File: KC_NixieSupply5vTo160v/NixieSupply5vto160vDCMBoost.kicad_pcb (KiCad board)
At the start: 2 copper layers, 38.2 x 37.9 mm, 47 parts, among them J1 Screw_Terminal_01x04, J2 CONN_01X01, J3 CONN_01X01, J4 CONN_01X01, J5 CONN_01X01, P1 USB_OTG, Q1 FDS2672CT, Q26 MMBTA42, U1 UCC3803

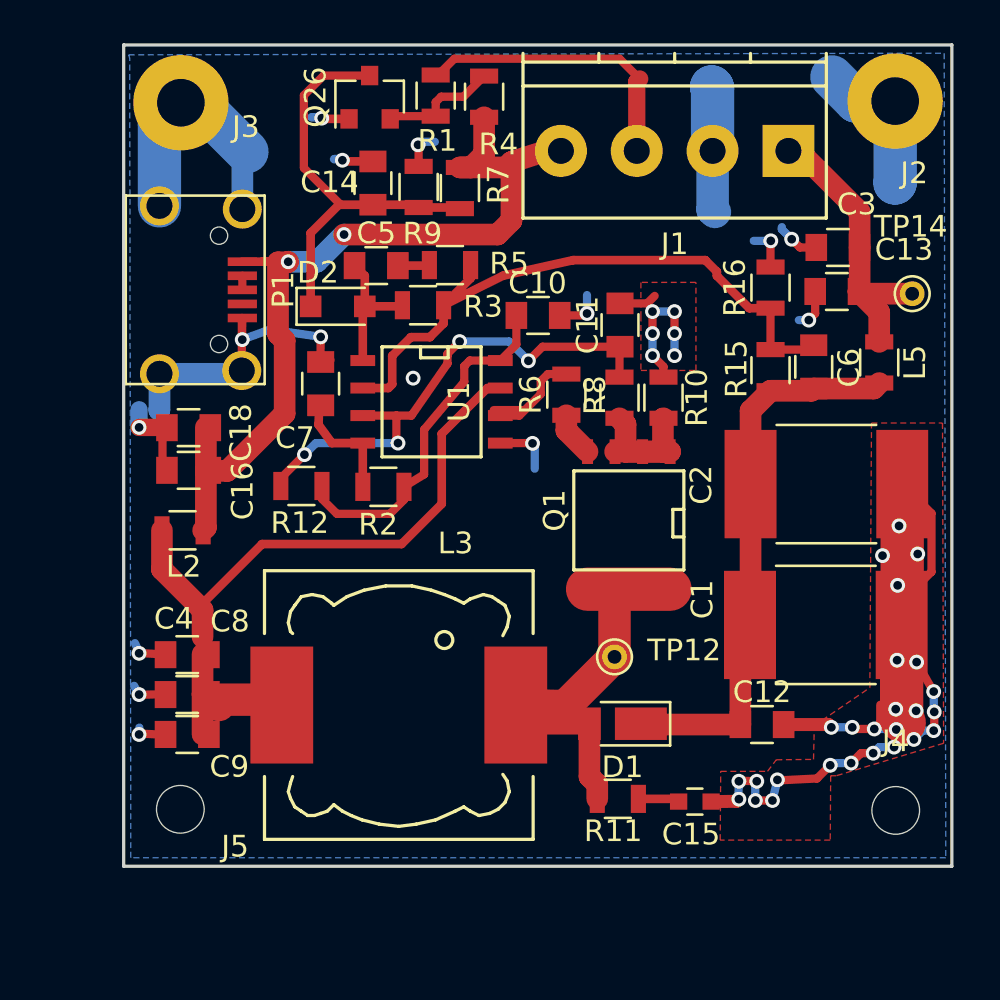
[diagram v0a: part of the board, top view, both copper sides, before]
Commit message: Latest updates for the verification Blog
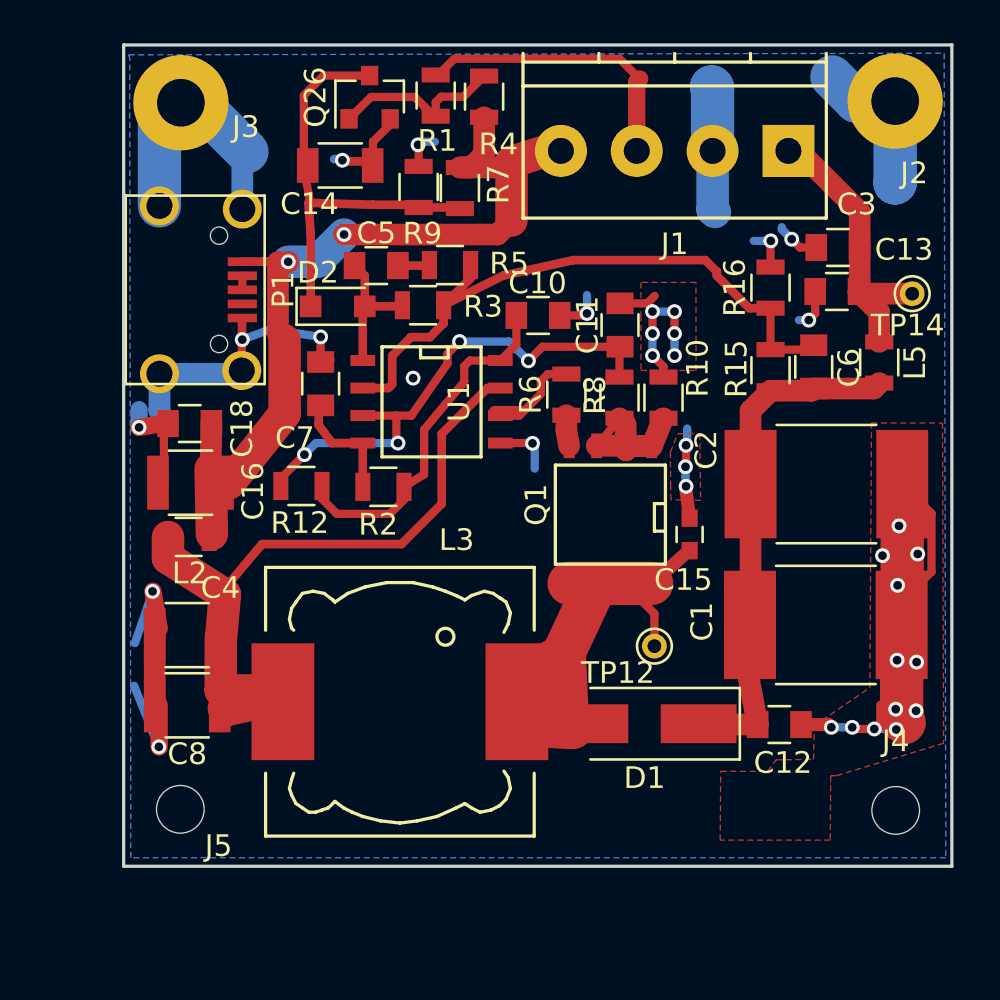
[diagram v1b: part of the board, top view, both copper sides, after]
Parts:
- removed C9: 47uF 10v, Capacitors_SMD:C_0805
- removed R11: 20 0.5W, Resistors_SMD:R_0805
- C14: value 47uF 10v -> 47uF 16v; footprint Capacitors_SMD:C_0805 -> Capacitors_SMD:C_1206
- C15: value 47pF 250v -> 560pF 250v
- C16, C4, C8: value 47uF 10v -> 100uF 16v; footprint Capacitors_SMD:C_0805 -> Capacitors_SMD:C_1210
- C7: value 330pF -> 430pF
- D1: value DFLS1200-7 -> ES1D; footprint Diodes_SMD:D_PowerDI-123 -> Diodes_SMD:D_SMA_Handsoldering
- Q26: value MMBTA42 -> MMBT42
- R12: value 8.2k -> 4.12k
- R6: value 10 -> 0 Ohm
- moved C15 12.3 mm to (162.2, 95.8), turned to 90 degrees
- moved TP12 1.91 mm to (160.6, 101.0)
- moved C14 1.72 mm to (146.1, 78.8), turned to 0 degrees
- moved D1 1.02 mm to (160.1, 104.5)
- moved C4 0.90 mm to (139.0, 100.4)
- moved Q1 0.89 mm to (158.5, 94.9)
- moved C12 0.80 mm to (166.3, 104.6)
- moved C16 0.58 mm to (139.2, 93.4)
- moved C8 0.50 mm to (139.0, 103.7)
- moved L2 0.41 mm to (139.1, 95.9)
- moved C18 0.20 mm to (139.1, 90.7)
- moved L3 0.16 mm to (148.8, 103.5)
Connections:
- D1 pad 2: Net-(D1-Pad2) -> Net-(C15-Pad1)
- L3 pad 1: Net-(D1-Pad2) -> Net-(C15-Pad1)
- Q1 pad 5: Net-(D1-Pad2) -> Net-(C15-Pad1)
- Q1 pad 6: Net-(D1-Pad2) -> Net-(C15-Pad1)
- Q1 pad 7: Net-(D1-Pad2) -> Net-(C15-Pad1)
- Q1 pad 8: Net-(D1-Pad2) -> Net-(C15-Pad1)
- Q26 pad 1: GND -> Net-(Q26-Pad1)
- Q26 pad 2: Net-(Q26-Pad2) -> GND
- R1 pad 1: Net-(Q26-Pad2) -> Net-(Q26-Pad1)
- R4 pad 1: Net-(Q26-Pad2) -> Net-(Q26-Pad1)
- TP12 pad 1: Net-(D1-Pad2) -> Net-(C15-Pad1)
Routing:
- net Net-(C15-Pad1): track 1.91 -> 33.9 mm
- net Net-(D1-Pad2): track 26.7 -> 0.00 mm
- net Net-(Q26-Pad1): track 0.00 -> 8.16 mm
- net Net-(Q26-Pad2): track 5.53 -> 0.00 mm
- net GND: track 148.7 -> 145.0 mm, vias 46 -> 33
- net Net-(C4-Pad1): track 42.9 -> 39.8 mm
- net 5v_Power: track 46.5 -> 47.9 mm
- net Net-(Q1-Pad4): track 2.08 -> 1.42 mm
